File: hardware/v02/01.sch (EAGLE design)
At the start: 31 parts, among them IC1 MSP430G2553, IC2 78L05Z, X2 RJ45-6L-B

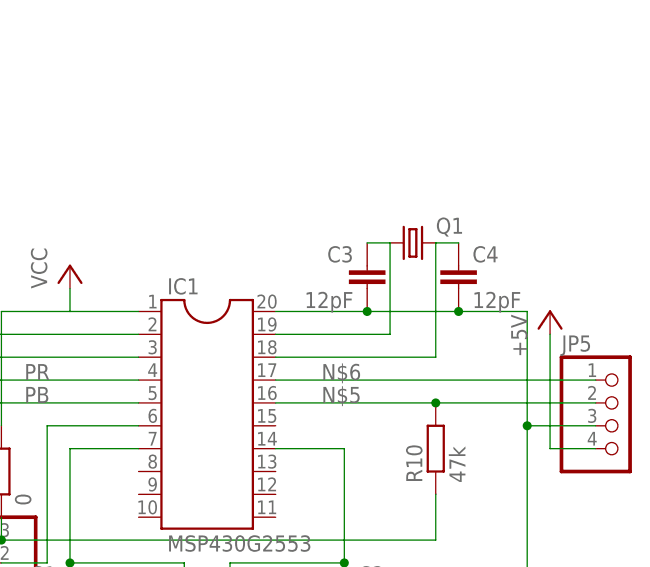
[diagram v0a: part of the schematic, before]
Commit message: XTAl flat on board; holes for additional wire
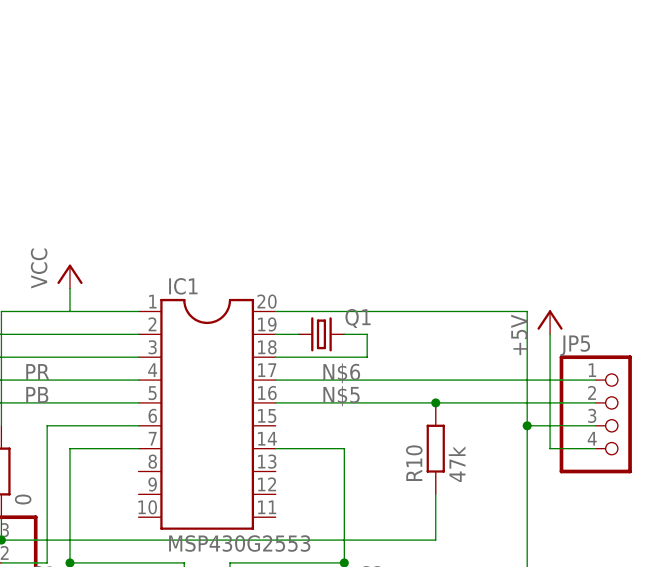
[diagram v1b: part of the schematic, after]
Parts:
- removed C3, C4: 12pF, rcl:C-EU025-024X044
- Q1: device crystal:CRYSTALTC26V -> crystal:CRYSTALTC26H
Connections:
- net GND: no longer C3.2, C4.2
- net N$2: no longer C3.1
- net N$7: no longer C4.1
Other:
- moved on the sheet: Q1
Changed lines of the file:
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@@
 <part name="C1" library="rcl" deviceset="C-EU" device="025-024X044" value="100nF"/>
 <part name="C2" library="rcl" deviceset="C-EU" device="025-024X044" value="100nF"/>
-<part name="Q1" library="crystal" deviceset="CRYSTAL" device="TC26V"/>
-<part name="C3" library="rcl" deviceset="C-EU" device="025-024X044" value="12pF"/>
+<part name="Q1" library="crystal" deviceset="CRYSTAL" device="TC26H"/>
 <part name="R8" library="rcl" deviceset="R-EU_" device="0207/10" value="470"/>
 <part name="R9" library="rcl" deviceset="R-EU_" device="0207/10" value="220"/>
@@
 <part name="P+8" library="supply1" deviceset="+5V" device=""/>
 <part name="GND4" library="supply1" deviceset="GND" device=""/>
-<part name="C4" library="rcl" deviceset="C-EU" device="025-024X044" value="12pF"/>
 <part name="R1" library="rcl" deviceset="R-EU_" device="0207/12" value="0"/>
 <part name="R10" library="rcl" deviceset="R-EU_" device="0207/10" value="47k"/>
@@
 <instance part="C1" gate="G$1" x="60.96" y="38.1" rot="MR0"/>
 <instance part="C2" gate="G$1" x="91.44" y="38.1"/>
-<instance part="Q1" gate="G$1" x="99.06" y="76.2"/>
-<instance part="C3" gate="G$1" x="93.98" y="73.66" rot="MR0"/>
+<instance part="Q1" gate="G$1" x="88.9" y="66.04"/>
 <instance part="R8" gate="G$1" x="0" y="38.1" rot="R180"/>
 <instance part="R9" gate="G$1" x="-10.16" y="48.26" rot="R90"/>
@@
 <instance part="P+8" gate="1" x="-27.94" y="106.68"/>
 <instance part="GND4" gate="1" x="-25.4" y="76.2"/>
-<instance part="C4" gate="G$1" x="104.14" y="73.66"/>
 <instance part="R1" gate="G$1" x="53.34" y="50.8" rot="R90"/>
 <instance part="R10" gate="G$1" x="101.6" y="53.34" rot="R90"/>
@@
 <wire x1="91.44" y1="30.48" x2="91.44" y2="33.02" width="0.1524" layer="91"/>
 <wire x1="111.76" y1="30.48" x2="91.44" y2="30.48" width="0.1524" layer="91"/>
-<wire x1="83.82" y1="68.58" x2="93.98" y2="68.58" width="0.1524" layer="91"/>
-<wire x1="93.98" y1="68.58" x2="104.14" y2="68.58" width="0.1524" layer="91"/>
-<wire x1="104.14" y1="68.58" x2="111.76" y2="68.58" width="0.1524" layer="91"/>
+<wire x1="83.82" y1="68.58" x2="111.76" y2="68.58" width="0.1524" layer="91"/>
 <wire x1="111.76" y1="68.58" x2="111.76" y2="55.88" width="0.1524" layer="91"/>
 <wire x1="111.76" y1="55.88" x2="111.76" y2="30.48" width="0.1524" layer="91"/>
@@
 <junction x="60.96" y="30.48"/>
 <junction x="91.44" y="30.48"/>
-<junction x="93.98" y="68.58"/>
 <junction x="76.2" y="30.48"/>
 <junction x="111.76" y="55.88"/>
-<junction x="104.14" y="68.58"/>
 <pinref part="GND1" gate="1" pin="GND"/>
 <pinref part="C1" gate="G$1" pin="2"/>
 <pinref part="C2" gate="G$1" pin="2"/>
 <pinref part="IC1" gate="G$1" pin="20"/>
-<pinref part="C3" gate="G$1" pin="2"/>
 <pinref part="JP3" gate="A" pin="1"/>
 <pinref part="JP4" gate="A" pin="2"/>
 <pinref part="JP5" gate="A" pin="3"/>
-<pinref part="C4" gate="G$1" pin="2"/>
 </segment>
 <segment>
@@
 <net name="N$2" class="0">
 <segment>
-<wire x1="96.52" y1="76.2" x2="93.98" y2="76.2" width="0.1524" layer="91"/>
-<wire x1="96.52" y1="76.2" x2="96.52" y2="66.04" width="0.1524" layer="91"/>
-<wire x1="96.52" y1="66.04" x2="83.82" y2="66.04" width="0.1524" layer="91"/>
-<pinref part="C3" gate="G$1" pin="1"/>
+<wire x1="86.36" y1="66.04" x2="83.82" y2="66.04" width="0.1524" layer="91"/>
 <pinref part="Q1" gate="G$1" pin="1"/>
 <pinref part="IC1" gate="G$1" pin="19"/>
@@
 <net name="N$7" class="0">
 <segment>
-<wire x1="101.6" y1="76.2" x2="104.14" y2="76.2" width="0.1524" layer="91"/>
-<wire x1="101.6" y1="76.2" x2="101.6" y2="63.5" width="0.1524" layer="91"/>
-<wire x1="101.6" y1="63.5" x2="83.82" y2="63.5" width="0.1524" layer="91"/>
+<wire x1="91.44" y1="66.04" x2="93.98" y2="66.04" width="0.1524" layer="91"/>
+<wire x1="93.98" y1="66.04" x2="93.98" y2="63.5" width="0.1524" layer="91"/>
+<wire x1="93.98" y1="63.5" x2="83.82" y2="63.5" width="0.1524" layer="91"/>
 <pinref part="Q1" gate="G$1" pin="2"/>
 <pinref part="IC1" gate="G$1" pin="18"/>
-<pinref part="C4" gate="G$1" pin="1"/>
-</segment>
-</net>
+</segment>
+</net>

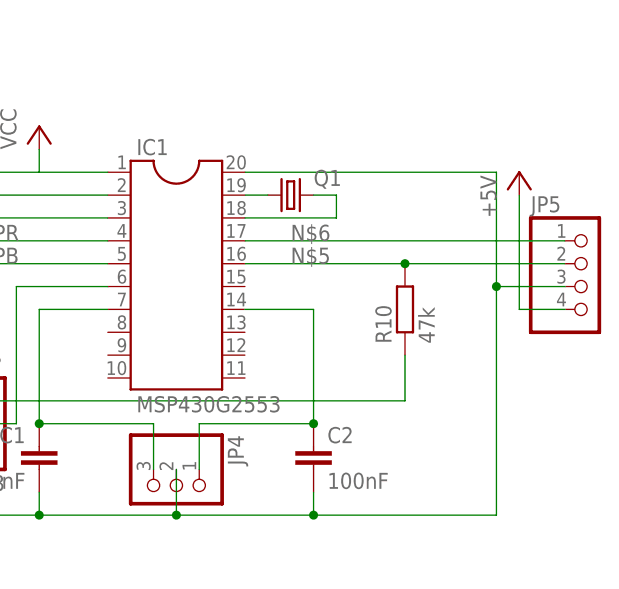
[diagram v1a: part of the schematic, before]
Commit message: C3 between RST and GND
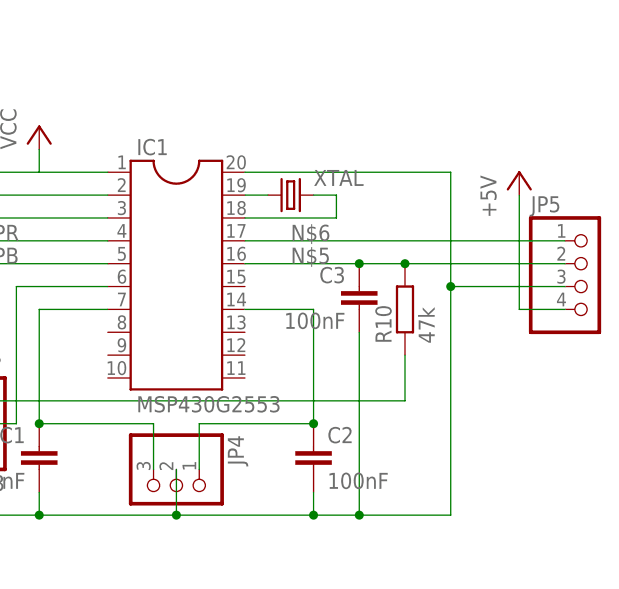
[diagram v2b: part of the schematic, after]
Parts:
- added C3: 100nF, rcl:C-EU025-024X044
- renumbered Q1 to XTAL
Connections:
- net GND: now also C3.2
- net N$5: now also C3.1
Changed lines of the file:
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@@
 <part name="C1" library="rcl" deviceset="C-EU" device="025-024X044" value="100nF"/>
 <part name="C2" library="rcl" deviceset="C-EU" device="025-024X044" value="100nF"/>
-<part name="Q1" library="crystal" deviceset="CRYSTAL" device="TC26H"/>
+<part name="XTAL" library="crystal" deviceset="CRYSTAL" device="TC26H"/>
 <part name="R8" library="rcl" deviceset="R-EU_" device="0207/10" value="470"/>
 <part name="R9" library="rcl" deviceset="R-EU_" device="0207/10" value="220"/>
@@
 <part name="R1" library="rcl" deviceset="R-EU_" device="0207/12" value="0"/>
 <part name="R10" library="rcl" deviceset="R-EU_" device="0207/10" value="47k"/>
+<part name="C3" library="rcl" deviceset="C-EU" device="025-024X044" value="100nF"/>
 </parts>
 <sheets>
@@
 <instance part="C1" gate="G$1" x="60.96" y="38.1" rot="MR0"/>
 <instance part="C2" gate="G$1" x="91.44" y="38.1"/>
-<instance part="Q1" gate="G$1" x="88.9" y="66.04"/>
+<instance part="XTAL" gate="G$1" x="88.9" y="66.04"/>
 <instance part="R8" gate="G$1" x="0" y="38.1" rot="R180"/>
 <instance part="R9" gate="G$1" x="-10.16" y="48.26" rot="R90"/>
@@
 <instance part="R1" gate="G$1" x="53.34" y="50.8" rot="R90"/>
 <instance part="R10" gate="G$1" x="101.6" y="53.34" rot="R90"/>
+<instance part="C3" gate="G$1" x="96.52" y="55.88" rot="MR0"/>
 </instances>
 <busses>
@@
 <wire x1="76.2" y1="30.48" x2="91.44" y2="30.48" width="0.1524" layer="91"/>
 <wire x1="91.44" y1="30.48" x2="91.44" y2="33.02" width="0.1524" layer="91"/>
-<wire x1="111.76" y1="30.48" x2="91.44" y2="30.48" width="0.1524" layer="91"/>
-<wire x1="83.82" y1="68.58" x2="111.76" y2="68.58" width="0.1524" layer="91"/>
-<wire x1="111.76" y1="68.58" x2="111.76" y2="55.88" width="0.1524" layer="91"/>
-<wire x1="111.76" y1="55.88" x2="111.76" y2="30.48" width="0.1524" layer="91"/>
+<wire x1="106.68" y1="30.48" x2="96.52" y2="30.48" width="0.1524" layer="91"/>
+<wire x1="96.52" y1="30.48" x2="91.44" y2="30.48" width="0.1524" layer="91"/>
+<wire x1="83.82" y1="68.58" x2="106.68" y2="68.58" width="0.1524" layer="91"/>
+<wire x1="106.68" y1="68.58" x2="106.68" y2="55.88" width="0.1524" layer="91"/>
+<wire x1="106.68" y1="55.88" x2="106.68" y2="30.48" width="0.1524" layer="91"/>
 <wire x1="53.34" y1="38.1" x2="53.34" y2="30.48" width="0.1524" layer="91"/>
 <wire x1="76.2" y1="35.56" x2="76.2" y2="30.48" width="0.1524" layer="91"/>
-<wire x1="119.38" y1="55.88" x2="111.76" y2="55.88" width="0.1524" layer="91"/>
+<wire x1="119.38" y1="55.88" x2="106.68" y2="55.88" width="0.1524" layer="91"/>
 <junction x="60.96" y="30.48"/>
 <junction x="91.44" y="30.48"/>
 <junction x="76.2" y="30.48"/>
-<junction x="111.76" y="55.88"/>
+<junction x="106.68" y="55.88"/>
 <pinref part="GND1" gate="1" pin="GND"/>
 <pinref part="C1" gate="G$1" pin="2"/>
@@
 <pinref part="JP4" gate="A" pin="2"/>
 <pinref part="JP5" gate="A" pin="3"/>
+<pinref part="C3" gate="G$1" pin="2"/>
+<wire x1="96.52" y1="50.8" x2="96.52" y2="30.48" width="0.1524" layer="91"/>
+<junction x="96.52" y="30.48"/>
 </segment>
 <segment>
@@
 <pinref part="JP5" gate="A" pin="2"/>
 <pinref part="R10" gate="G$1" pin="2"/>
-<wire x1="101.6" y1="58.42" x2="83.82" y2="58.42" width="0.1524" layer="91"/>
+<wire x1="101.6" y1="58.42" x2="96.52" y2="58.42" width="0.1524" layer="91"/>
 <junction x="101.6" y="58.42"/>
 <label x="88.9" y="58.42" size="1.778" layer="95"/>
+<pinref part="C3" gate="G$1" pin="1"/>
+<wire x1="96.52" y1="58.42" x2="83.82" y2="58.42" width="0.1524" layer="91"/>
+<junction x="96.52" y="58.42"/>
 </segment>
 </net>
@@
 <segment>
 <wire x1="86.36" y1="66.04" x2="83.82" y2="66.04" width="0.1524" layer="91"/>
-<pinref part="Q1" gate="G$1" pin="1"/>
+<pinref part="XTAL" gate="G$1" pin="1"/>
 <pinref part="IC1" gate="G$1" pin="19"/>
 </segment>
@@
 <wire x1="93.98" y1="66.04" x2="93.98" y2="63.5" width="0.1524" layer="91"/>
 <wire x1="93.98" y1="63.5" x2="83.82" y2="63.5" width="0.1524" layer="91"/>
-<pinref part="Q1" gate="G$1" pin="2"/>
+<pinref part="XTAL" gate="G$1" pin="2"/>
 <pinref part="IC1" gate="G$1" pin="18"/>
 </segment>

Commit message: C4 between Vcc and GND
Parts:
- removed C6: 100nF, rcl:C-EU025-024X044
- added C4: 200nF, rcl:CPOL-EUB45181A
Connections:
- net GND: now also C4.-; no longer C6.2
- net VCC: now also C4.+; no longer C6.1
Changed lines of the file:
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@@
 <part name="JP4" library="pinhead" deviceset="PINHD-1X3" device=""/>
 <part name="JP5" library="pinhead" deviceset="PINHD-1X4" device="/90"/>
-<part name="C6" library="rcl" deviceset="C-EU" device="025-024X044" value="100nF"/>
 <part name="X2" library="con-tycoelectronics" deviceset="RJ45" device="" technology="-6L-B"/>
 <part name="P+8" library="supply1" deviceset="+5V" device=""/>
@@
 <part name="R10" library="rcl" deviceset="R-EU_" device="0207/10" value="47k"/>
 <part name="C3" library="rcl" deviceset="C-EU" device="025-024X044" value="100nF"/>
+<part name="C4" library="rcl" deviceset="CPOL-EU" device="B45181A" value="200nF"/>
 </parts>
 <sheets>
@@
 <instance part="JP4" gate="A" x="76.2" y="33.02" rot="R270"/>
 <instance part="JP5" gate="A" x="121.92" y="55.88"/>
-<instance part="C6" gate="G$1" x="40.64" y="116.84"/>
 <instance part="X2" gate="G$1" x="-35.56" y="93.98" rot="R180"/>
 <instance part="P+8" gate="1" x="-27.94" y="106.68"/>
@@
 <instance part="R10" gate="G$1" x="101.6" y="53.34" rot="R90"/>
 <instance part="C3" gate="G$1" x="96.52" y="55.88" rot="MR0"/>
+<instance part="C4" gate="G$1" x="40.64" y="116.84"/>
 </instances>
 <busses>
@@
 <pinref part="IC2" gate="A1" pin="VO"/>
 <pinref part="P+7" gate="VCC" pin="VCC"/>
-<pinref part="C6" gate="G$1" pin="1"/>
+<pinref part="C4" gate="G$1" pin="+"/>
 </segment>
 </net>
@@
 <pinref part="GND6" gate="1" pin="GND"/>
 <pinref part="C5" gate="G$1" pin="-"/>
-<pinref part="C6" gate="G$1" pin="2"/>
+<pinref part="C4" gate="G$1" pin="-"/>
 </segment>
 <segment>

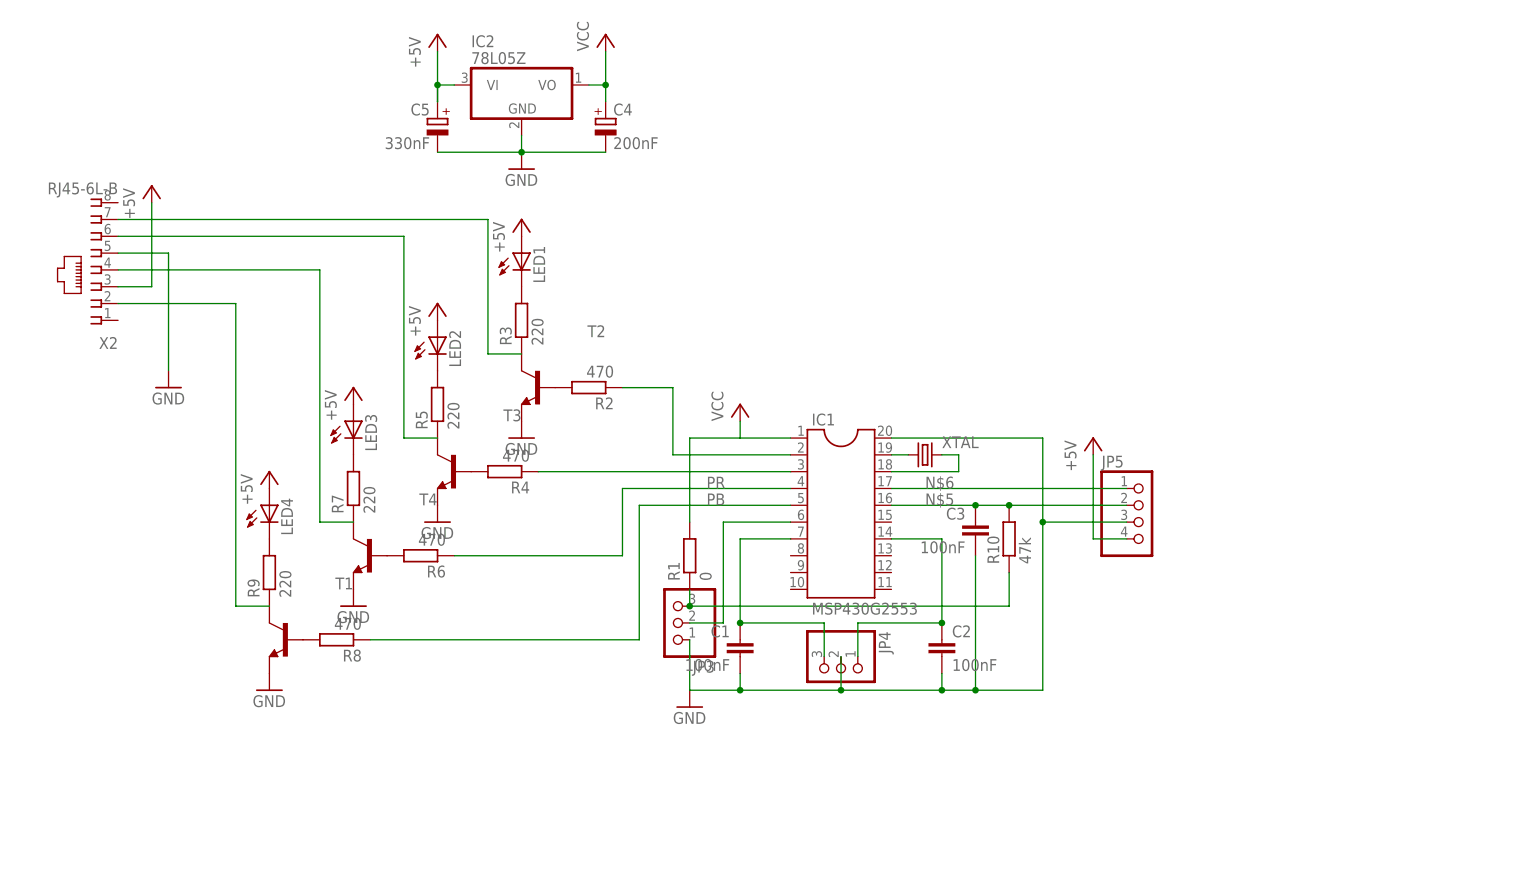
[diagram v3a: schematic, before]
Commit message: rearranged transistorsand LEDs; additional resistors; pre final version
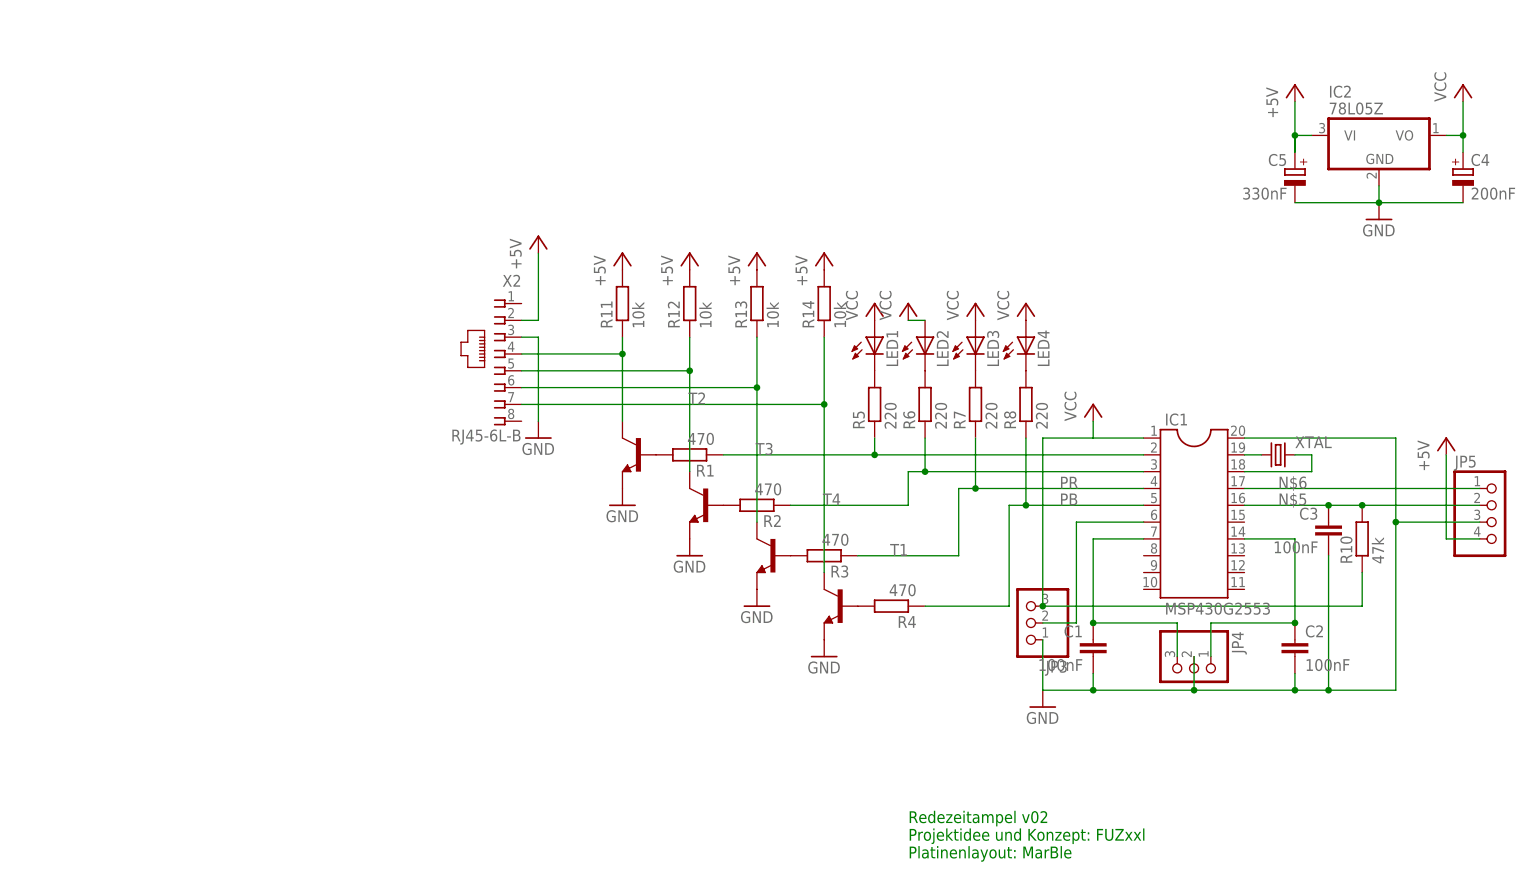
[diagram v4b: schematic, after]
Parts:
- removed R9: 220, rcl:R-EU_0207/10
- added R11, R12, R13, R14: 10k, rcl:R-EU_0207/10
- R1: value 0 -> 470; device rcl:R-EU_0207/12 -> rcl:R-EU_0207/10
- R3: value 220 -> 470
- R6, R8: value 470 -> 220
- T1, T2, T3, T4: device transistor:-NPN-TO92 -> transistor:-NPN-TO92-EBC
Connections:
- removed net N$10: R9.1, T1.C, X2.2
- removed net N$14: R3.1, T2.C, X2.7
- removed net N$15: JP3.3, R1.1, R10.1
- removed net N$19: R5.1, T3.C, X2.6
- removed net N$22: R7.1, T4.C, X2.4
- new net N$27: R14.1, T1.C, X2.7
- new net N$28: R13.1, T4.C, X2.6
- new net N$29: R12.1, T3.C, X2.5
- new net N$30: R11.1, T2.C, X2.4
- net +5V: now also R11.2, R12.2, R13.2, R14.2, X2.2; no longer LED1.A, LED2.A, LED3.A, LED4.A, X2.3
- net GND: now also X2.3; no longer X2.5
- net N$11: now also R4.2; no longer R8.2
- net N$12: now also R1.1, R5.1; no longer R2.1
- net N$13: now also R5.2; no longer R3.2
- net N$16: now also R1.2; no longer R2.2
- net N$17: now also R6.2; no longer R5.2
- net N$20: now also R2.2; no longer R4.2
- net N$23: now also R3.2; no longer R6.2
- net N$8: now also R8.2; no longer R9.2
- net N$9: now also R2.1, R6.1; no longer R4.1
- net PB: now also R4.1
- net PR: now also R3.1, R7.1; no longer R6.1
- net VCC: now also JP3.3, LED1.A, LED2.A, LED3.A, LED4.A, R10.1; no longer R1.2
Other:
- note added: "Redezeitampel v02 Projektidee und Konzept: FUZxxl Platinenlayout: MarBle"
- moved on the sheet: C1, C2, C3, C4, C5, IC1, IC2, JP3, JP4, JP5, LED1, LED2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
